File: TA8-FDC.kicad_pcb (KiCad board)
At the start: 2 copper layers, 170 x 105.2 mm, 68 parts, among them IC101 SED9420C, IC102 LS74, IC103 LS32, IC104 74LS95, IC105 LS10, IC106 LS139, IC107 74LS641, IC108 LS368, IC109 LS08, IC110 LS02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

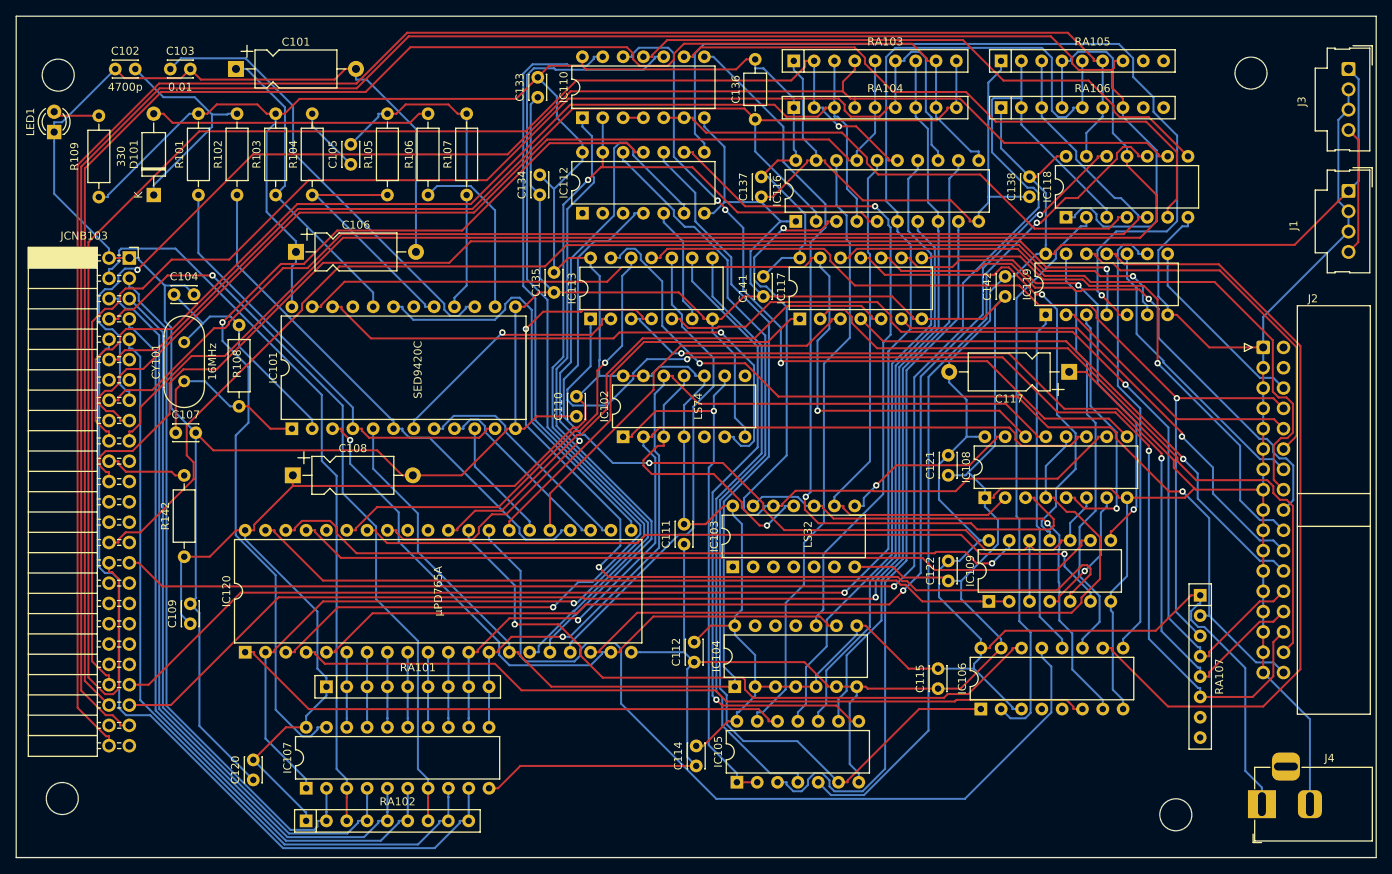
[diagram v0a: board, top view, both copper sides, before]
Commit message: Add files via upload
corrected a couple of error on schematics
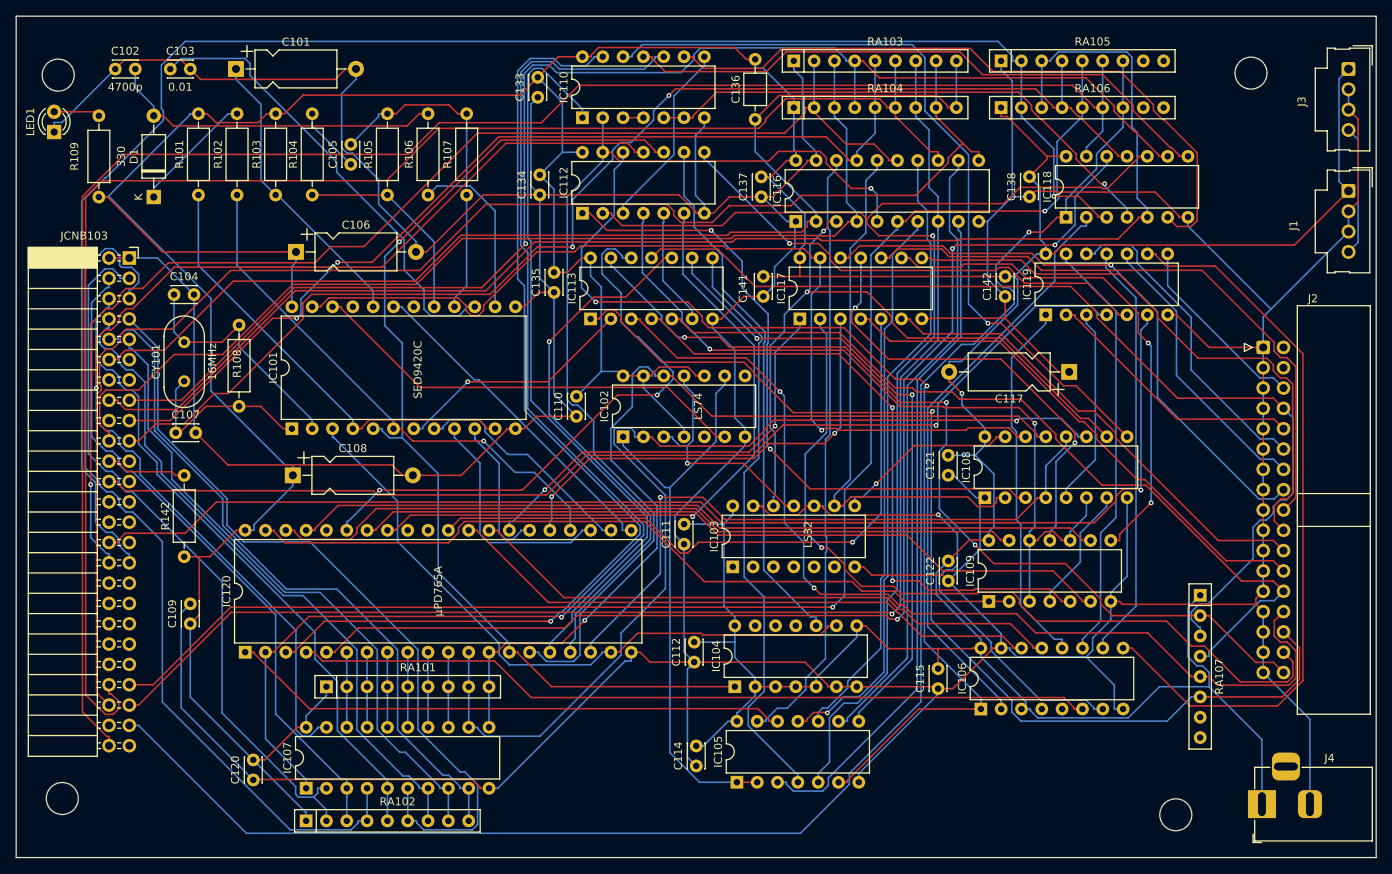
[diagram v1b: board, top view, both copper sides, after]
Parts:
- removed D101: IS2473, Diode_THT:D_A-405_P10.16mm_Horizontal
- added D1: IS2473, Diode_THT:D_A-405_P10.16mm_Horizontal, F.Cu at (123.2, 59.4)
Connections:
- C102 pad 2: Net-(D101-K) -> Net-(D1-A)
- IC105 pad 5: Net-(IC105-Pad5) -> /toIORQ
- IC110 pad 8: Net-(IC108-Pad3) -> Net-(IC110-Pad8)
- IC112 pad 1: unconnected-(IC112-Pad1) -> Net-(IC108-Pad3)
- IC112 pad 2: unconnected-(IC112-Pad2) -> /toIORQ
- IC112 pad 3: unconnected-(IC112-Pad3) -> Net-(IC110-Pad8)
- IC118 pad 10: Net-(IC105-Pad5) -> /toIORQ
- R102 pad 2: Net-(D101-K) -> Net-(D1-K)
- R106 pad 2: Net-(D101-A) -> Net-(D1-A)
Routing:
- net /toIORQ: track 0.00 -> 158.2 mm, vias 0 -> 1
- net Net-(IC105-Pad5): track 105.7 -> 0.00 mm, vias 1 -> 0
- net Net-(IC112-Pad8): track 113.2 -> 62.6 mm
- net Net-(IC106B-O2): track 99.4 -> 52.6 mm
- net Net-(IC109-Pad5): track 122.5 -> 79.9 mm
- net /~{DACK2}: track 195.7 -> 153.1 mm
- net Net-(D1-A): track 0.00 -> 42.2 mm
- net /A3: track 248.4 -> 207.6 mm, vias 0 -> 1
- net Net-(IC106B-O3): track 56.4 -> 92.4 mm
- net Net-(D101-A): track 35.2 -> 0.00 mm
- net /us1: track 110.4 -> 75.4 mm
- net Net-(D101-K): track 28.2 -> 0.00 mm
- net Net-(IC110-Pad8): track 0.00 -> 23.8 mm
- net GND: track 853.7 -> 831.2 mm
- net /A7: track 204.8 -> 183.6 mm, vias 1 -> 2
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
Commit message: Fixed C117
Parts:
- C117: value 10µF -> 10uF
- moved C117 15.0 mm to (222.6, 81.3), turned to 0 degrees
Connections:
- C117 pad 1: GND -> +5V
- C117 pad 2: +5V -> GND
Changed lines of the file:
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@@
   )
   (footprint "Capacitor_THT:CP_Axial_L10.0mm_D4.5mm_P15.00mm_Horizontal" (layer "F.Cu")
-    (at 237.624 81.2915 180)
+    (at 222.624 81.2685)
     (descr "CP, Axial series, Axial, Horizontal, pin pitch=15mm, , length*diameter=10*4.5mm^2, Electrolytic Capacitor, , http://www.vishay.com/docs/28325/021asm.pdf")
     (tags "CP Axial series Axial Horizontal pin pitch 15mm  length 10mm diameter 4.5mm Electrolytic Capacitor")
     (property "Sheetfile" "TA8-FDC.kicad_sch")
     (property "Sheetname" "")
-    (property "ki_description" "Unpolarized capacitor")
+    (property "ki_description" "Polarized capacitor")
     (property "ki_keywords" "cap capacitor")
     (attr through_hole)
@@
         (effects (font (size 1 1) (thickness 0.15)))
     )
-    (fp_text value "10µF" (at 7.5 3.37) (layer "F.Fab") hide
+    (fp_text value "10uF" (at 7.5 3.37) (layer "F.Fab") hide
         (effects (font (size 1 1) (thickness 0.15)))
     )
@@
     (fp_line (start 15 0) (end 12.5 0)
       (stroke (width 0.1) (type solid)) (layer "F.Fab"))
-    (pad "1" thru_hole rect (at 0 0 180) (size 2 2) (drill 1) (layers "*.Cu" "*.Mask")
+    (pad "1" thru_hole rect (at 0 0) (size 2 2) (drill 1) (layers "*.Cu" "*.Mask")
+      (net 1 "+5V") (pintype "passive"))
+    (pad "2" thru_hole oval (at 15 0) (size 2 2) (drill 1) (layers "*.Cu" "*.Mask")
       (net 4 "GND") (pintype "passive"))
-    (pad "2" thru_hole oval (at 15 0 180) (size 2 2) (drill 1) (layers "*.Cu" "*.Mask")
-      (net 1 "+5V") (pintype "passive"))
     (model "${KICAD6_3DMODEL_DIR}/Capacitor_THT.3dshapes/CP_Axial_L10.0mm_D4.5mm_P15.00mm_Horizontal.wrl"
       (offset (xyz 0 0 0))
